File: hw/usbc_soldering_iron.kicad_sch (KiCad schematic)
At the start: 85 parts, among them J1 USB_C_Receptacle_USB2.0_14P, J10 TIP_L, J11 TIP_H, J12 TIP_K, J13 TIP_L, J14 TIP_H, J15 TIP_K, J16 TIP_L, J2 DBG, J3 LED RING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

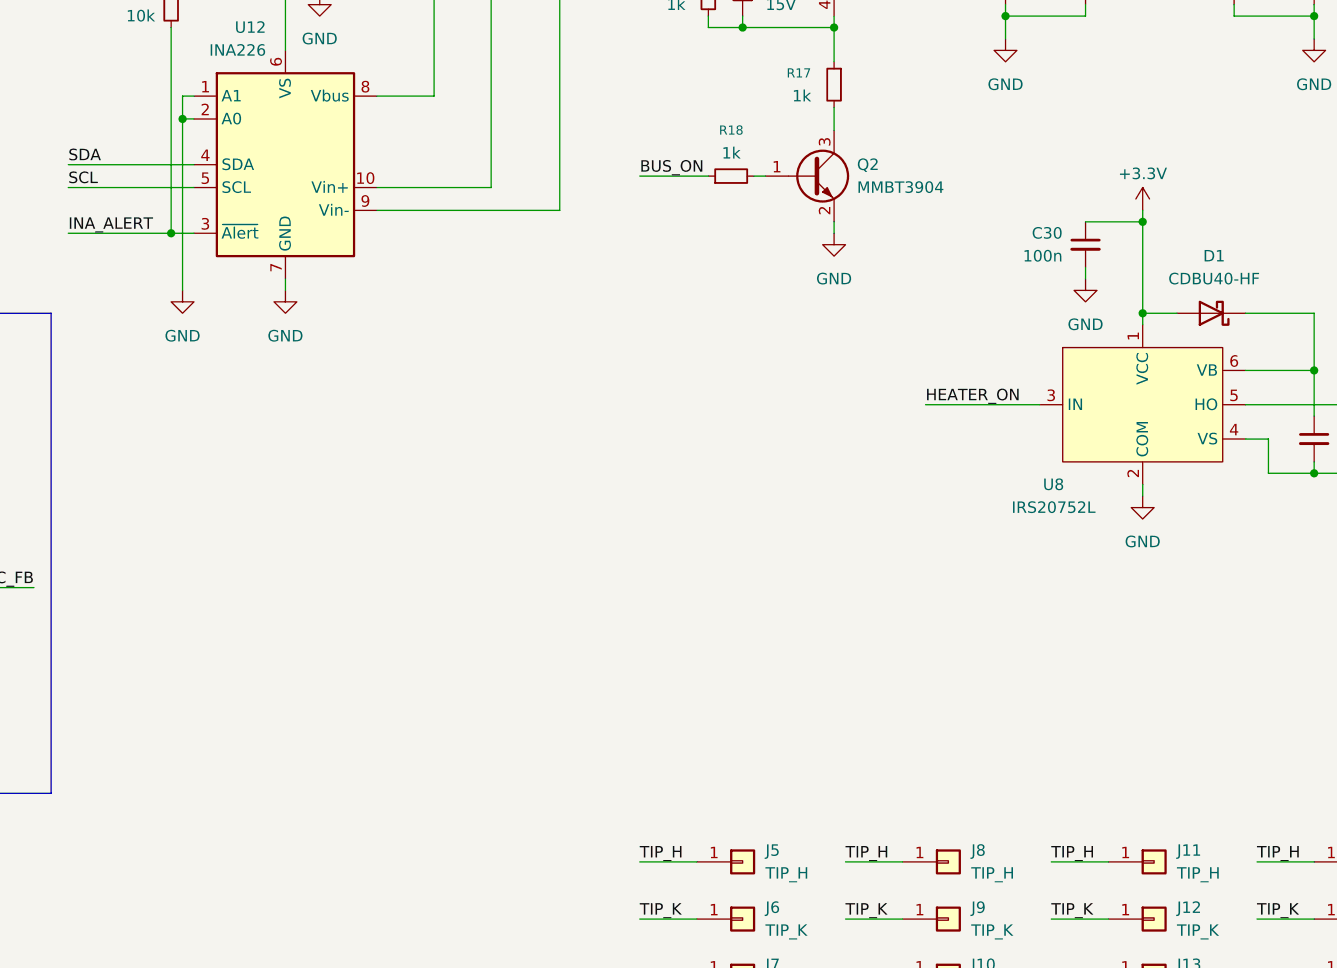
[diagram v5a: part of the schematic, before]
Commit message: separate boost for gate driver
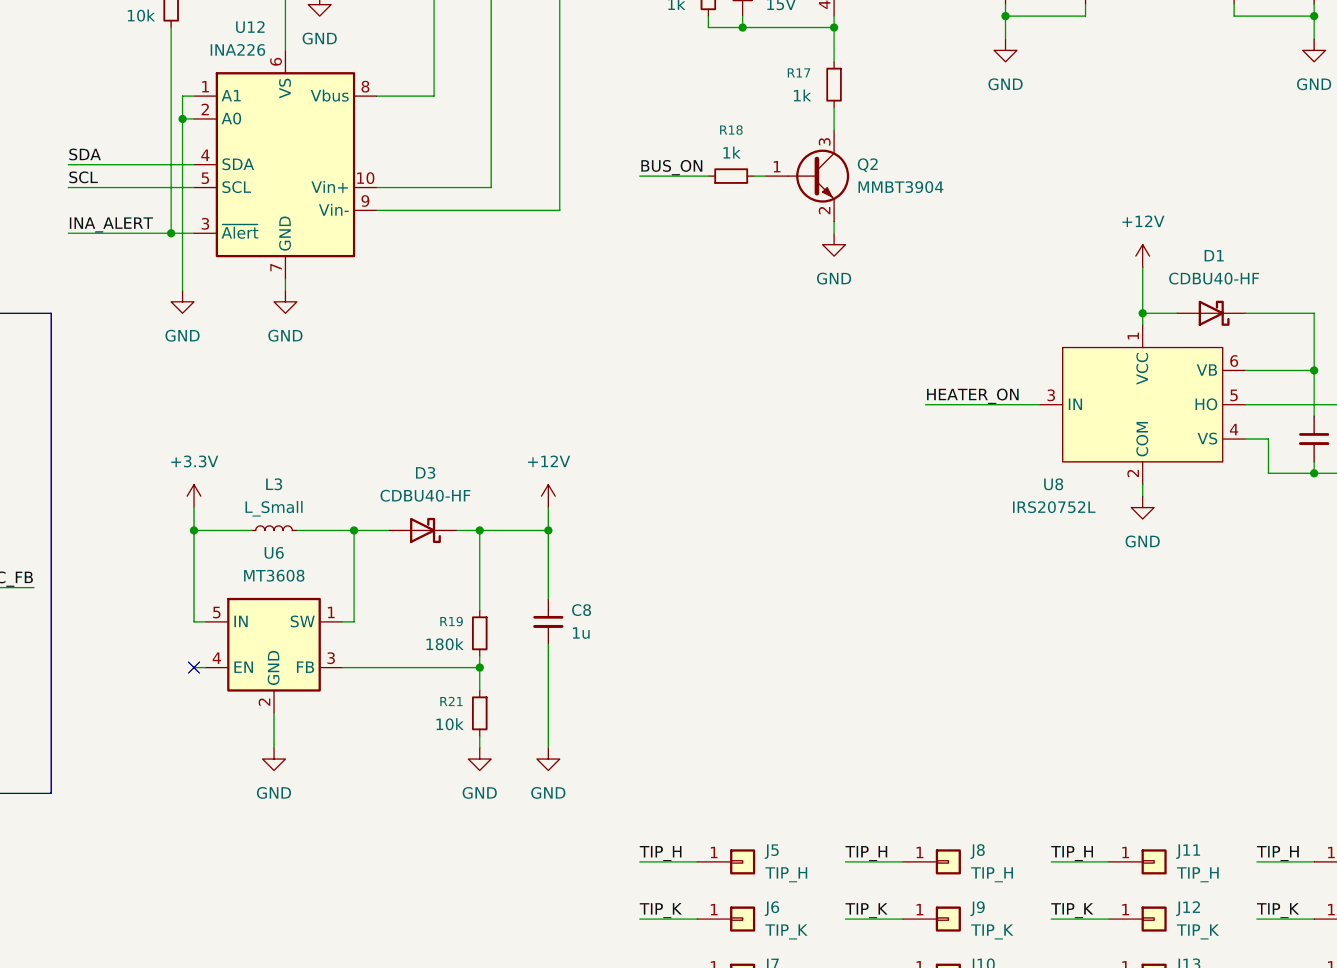
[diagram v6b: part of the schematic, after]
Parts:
- removed C30: 100n, Capacitor_SMD:C_0603_1608Metric, symbol Device:C_Small
- added C8: 1u, Capacitor_SMD:C_0603_1608Metric, symbol Device:C_Small
- added D3: CDBU40-HF, Diode_SMD:D_0603_1608Metric, symbol Diode:CDBU40-HF
- added L3: L_Small, Inductor_SMD:L_0603_1608Metric, symbol Device:L_Small
- added R19: 180k, Resistor_SMD:R_0603_1608Metric, symbol Device:R_Small
- added R21: 10k, Resistor_SMD:R_0603_1608Metric, symbol Device:R_Small
- added U6: MT3608, Package_TO_SOT_SMD:SOT-23-6, symbol Regulator_Switching:MT3608
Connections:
- net +3.3V: now also L3.1, U6.5 (IN); no longer D1.2 (A), U8.1 (VCC)
- net GND: now also C8.2, R21.2, U6.2 (GND)
- new net: D3.2 (A), L3.2, U6.1 (SW)
- new net: R19.2, R21.1, U6.3 (FB)
- new net +12V: C8.1, D1.2 (A), D3.1 (K), R19.1, U8.1 (VCC)
- no-connect marks 8 -> 9

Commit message: removed i2c temp sensor and high side bus switch
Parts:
- removed D2: 15V, Diode_SMD:D_SOD-323, symbol Device:D_Zener_Small
- removed Q2: MMBT3904, Package_TO_SOT_SMD:SOT-23, symbol Transistor_BJT:MMBT3904
- removed R17, R18: 1k, Resistor_SMD:R_0603_1608Metric, symbol Device:R_Small
- removed U10: CSD25402Q3A, Package_SON:VSON-8_3.3x3.3mm_P0.65mm_NexFET, symbol Transistor_FET:CSD25402Q3A
- removed U9: TMP102xxDRL, Package_TO_SOT_SMD:SOT-563, symbol Sensor_Temperature:TMP102xxDRL
- added TH1: 10k, Resistor_SMD:R_0603_1608Metric, symbol Device:Thermistor_NTC
- L3: value L_Small -> 4.7u
- R11: value 1k -> 1k 0.1%
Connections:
- net BUS_ON is gone; now on net HEATER_ON: U1.11 (PA5)
- net +3.3V: now also R11.1; no longer C22.1
- net GND: now also TH1.2
- net HEATER_ON: no longer U1.12 (PA6)
- net at R10.2, U12.9 (Vin-): now also C23.1, C25.1, L2.1; no longer R11.1
- net NTC: now reaches R11.2
- net NTC: now also C22.1, U1.7 (PA1), TH1.1
- net VDRIVE_ON: now reaches U6.4 (EN)
- net VDRIVE_ON: now also U1.10 (PA4)
- net +12V renamed VDRIVE
- no-connect marks 9 -> 7
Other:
- moved on the sheet: C22, C29, C8, D1, D3, L3, Q1, R19, R21, U6, U8

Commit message: preliminary BOM and schematic
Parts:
- R11: value 1k 0.1% -> 1k
- U8: value IRS20752L -> IRS20752L, IRS20752L, NSG10752
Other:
- moved on the sheet: C26, C28
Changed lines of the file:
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@@
 	)
 	(junction
-		(at 374.65 124.46)
+		(at 373.38 124.46)
 		(diameter 0)
 		(color 0 0 0 0)
@@
 	)
 	(junction
-		(at 365.76 116.84)
+		(at 364.49 116.84)
 		(diameter 0)
 		(color 0 0 0 0)
 	)
 	(junction
-		(at 374.65 116.84)
+		(at 373.38 116.84)
 		(diameter 0)
 		(color 0 0 0 0)
@@
 	(wire
 		(pts
-			(xy 374.65 116.84) (xy 374.65 118.11)
+			(xy 373.38 116.84) (xy 373.38 118.11)
 		)
 		(stroke
@@
 	(wire
 		(pts
-			(xy 374.65 124.46) (xy 374.65 127)
+			(xy 373.38 124.46) (xy 373.38 127)
 		)
 		(stroke
@@
 	(wire
 		(pts
-			(xy 374.65 116.84) (xy 389.89 116.84)
+			(xy 373.38 116.84) (xy 389.89 116.84)
 		)
 		(stroke
@@
 	(wire
 		(pts
-			(xy 374.65 123.19) (xy 374.65 124.46)
+			(xy 373.38 123.19) (xy 373.38 124.46)
 		)
 		(stroke
@@
 	(wire
 		(pts
-			(xy 365.76 116.84) (xy 365.76 118.11)
+			(xy 364.49 116.84) (xy 364.49 118.11)
 		)
 		(stroke
@@
 	(wire
 		(pts
-			(xy 365.76 123.19) (xy 365.76 124.46)
+			(xy 364.49 123.19) (xy 364.49 124.46)
 		)
 		(stroke
@@
 	(wire
 		(pts
-			(xy 365.76 124.46) (xy 374.65 124.46)
+			(xy 364.49 124.46) (xy 373.38 124.46)
 		)
 		(stroke
@@
 	(wire
 		(pts
-			(xy 365.76 116.84) (xy 374.65 116.84)
+			(xy 364.49 116.84) (xy 373.38 116.84)
 		)
 		(stroke
@@
 	(wire
 		(pts
-			(xy 360.68 116.84) (xy 365.76 116.84)
+			(xy 360.68 116.84) (xy 364.49 116.84)
 		)
 		(stroke
@@
 		(dnp no)
 		(property "Reference" "U8"
-			(at 349.25 162.052 0)
+			(at 350.52 164.592 0)
 			(effects
 				(font
@@
 			)
 		)
-		(property "Value" "IRS20752L"
-			(at 349.25 164.592 0)
+		(property "Value" "IRS20752L, IRS20752L, NSG10752"
+			(at 359.156 190.754 0)
 			(effects
 				(font
@@
 	(symbol
 		(lib_id "power:GND")
-		(at 374.65 127 0)
+		(at 373.38 127 0)
 		(unit 1)
 		(exclude_from_sim no)
@@
 		(fields_autoplaced yes)
 		(property "Reference" "#PWR041"
-			(at 374.65 133.35 0)
+			(at 373.38 133.35 0)
 			(effects
 				(font
@@
 		)
 		(property "Value" "GND"
-			(at 374.65 132.08 0)
+			(at 373.38 132.08 0)
 			(effects
 				(font
@@
 		)
 		(property "Footprint" ""
-			(at 374.65 127 0)
+			(at 373.38 127 0)
 			(effects
 				(font
@@
 		)
 		(property "Datasheet" ""
-			(at 374.65 127 0)
+			(at 373.38 127 0)
 			(effects
 				(font
@@
 		)
 		(property "Description" "Power symbol creates a global label with name \"GND\" , ground"
-			(at 374.65 127 0)
+			(at 373.38 127 0)
 			(effects
 				(font
@@
 			)
 		)
-		(property "Value" "1k 0.1%"
+		(property "Value" "1k"
 			(at 183.896 238.76 0)
 			(effects
@@
 	(symbol
 		(lib_id "Device:C_Small")
-		(at 374.65 120.65 0)
+		(at 373.38 120.65 0)
 		(unit 1)
 		(exclude_from_sim no)
@@
 		(fields_autoplaced yes)
 		(property "Reference" "C28"
-			(at 377.19 119.3862 0)
+			(at 375.92 119.3862 0)
 			(effects
 				(font
@@
 		)
 		(property "Value" "22u"
-			(at 377.19 121.9262 0)
+			(at 375.92 121.9262 0)
 			(effects
 				(font
@@
 		)
 		(property "Footprint" "Capacitor_SMD:C_0805_2012Metric"
-			(at 374.65 120.65 0)
+			(at 373.38 120.65 0)
 			(effects
 				(font
@@
 		)
 		(property "Datasheet" "~"
-			(at 374.65 120.65 0)
+			(at 373.38 120.65 0)
 			(effects
 				(font
@@
 		)
 		(property "Description" "Unpolarized capacitor, small symbol"
-			(at 374.65 120.65 0)
+			(at 373.38 120.65 0)
 			(effects
 				(font
@@
 	(symbol
 		(lib_id "Device:C_Small")
-		(at 365.76 120.65 0)
+		(at 364.49 120.65 0)
 		(unit 1)
 		(exclude_from_sim no)
@@
 		(fields_autoplaced yes)
 		(property "Reference" "C26"
-			(at 368.3 119.3862 0)
+			(at 367.03 119.3862 0)
 			(effects
 				(font
@@
 		)
 		(property "Value" "22u"
-			(at 368.3 121.9262 0)
+			(at 367.03 121.9262 0)
 			(effects
 				(font
@@
 		)
 		(property "Footprint" "Capacitor_SMD:C_0805_2012Metric"
-			(at 365.76 120.65 0)
+			(at 364.49 120.65 0)
 			(effects
 				(font
@@
 		)
 		(property "Datasheet" "~"
-			(at 365.76 120.65 0)
+			(at 364.49 120.65 0)
 			(effects
 				(font
@@
 		)
 		(property "Description" "Unpolarized capacitor, small symbol"
-			(at 365.76 120.65 0)
+			(at 364.49 120.65 0)
 			(effects
 				(font
